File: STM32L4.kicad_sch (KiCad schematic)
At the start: 37 parts, among them J1 Conn_01x04_Pin, U20 TCAN334GDCNT, U21 STM32L496RGTx, U8 TCAN334GDCNT, U9 MR20H40, Y1 8 MHZ Oscillator

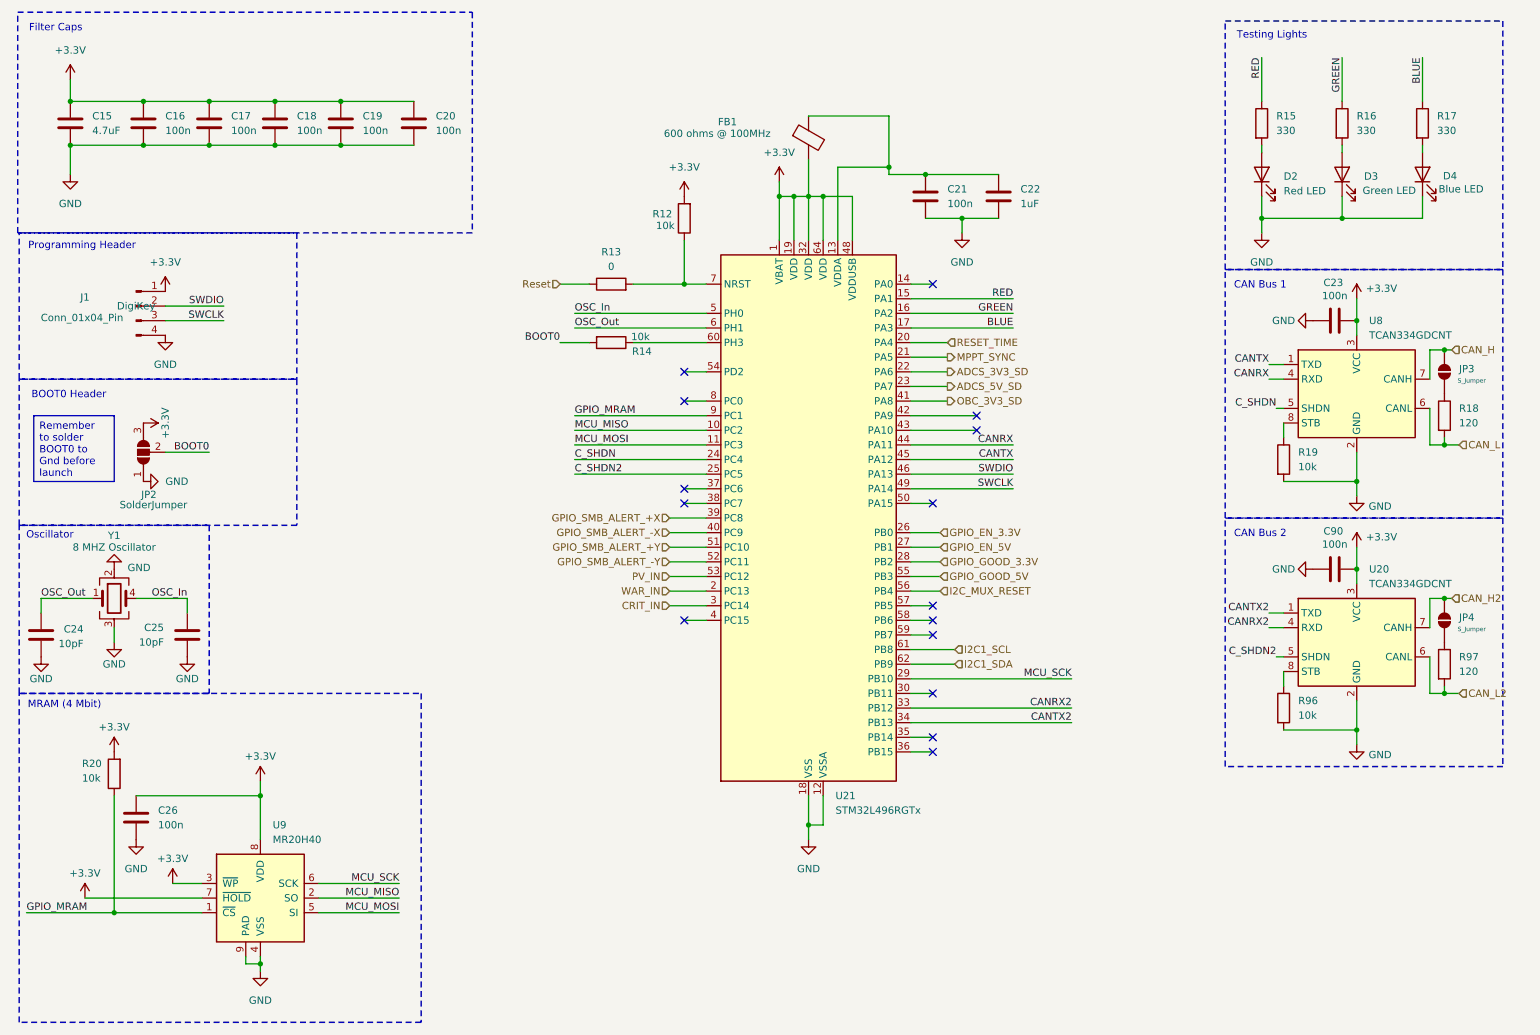
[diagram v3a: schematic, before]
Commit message: Changed LTC 4412 to 4417, still kinks to work out
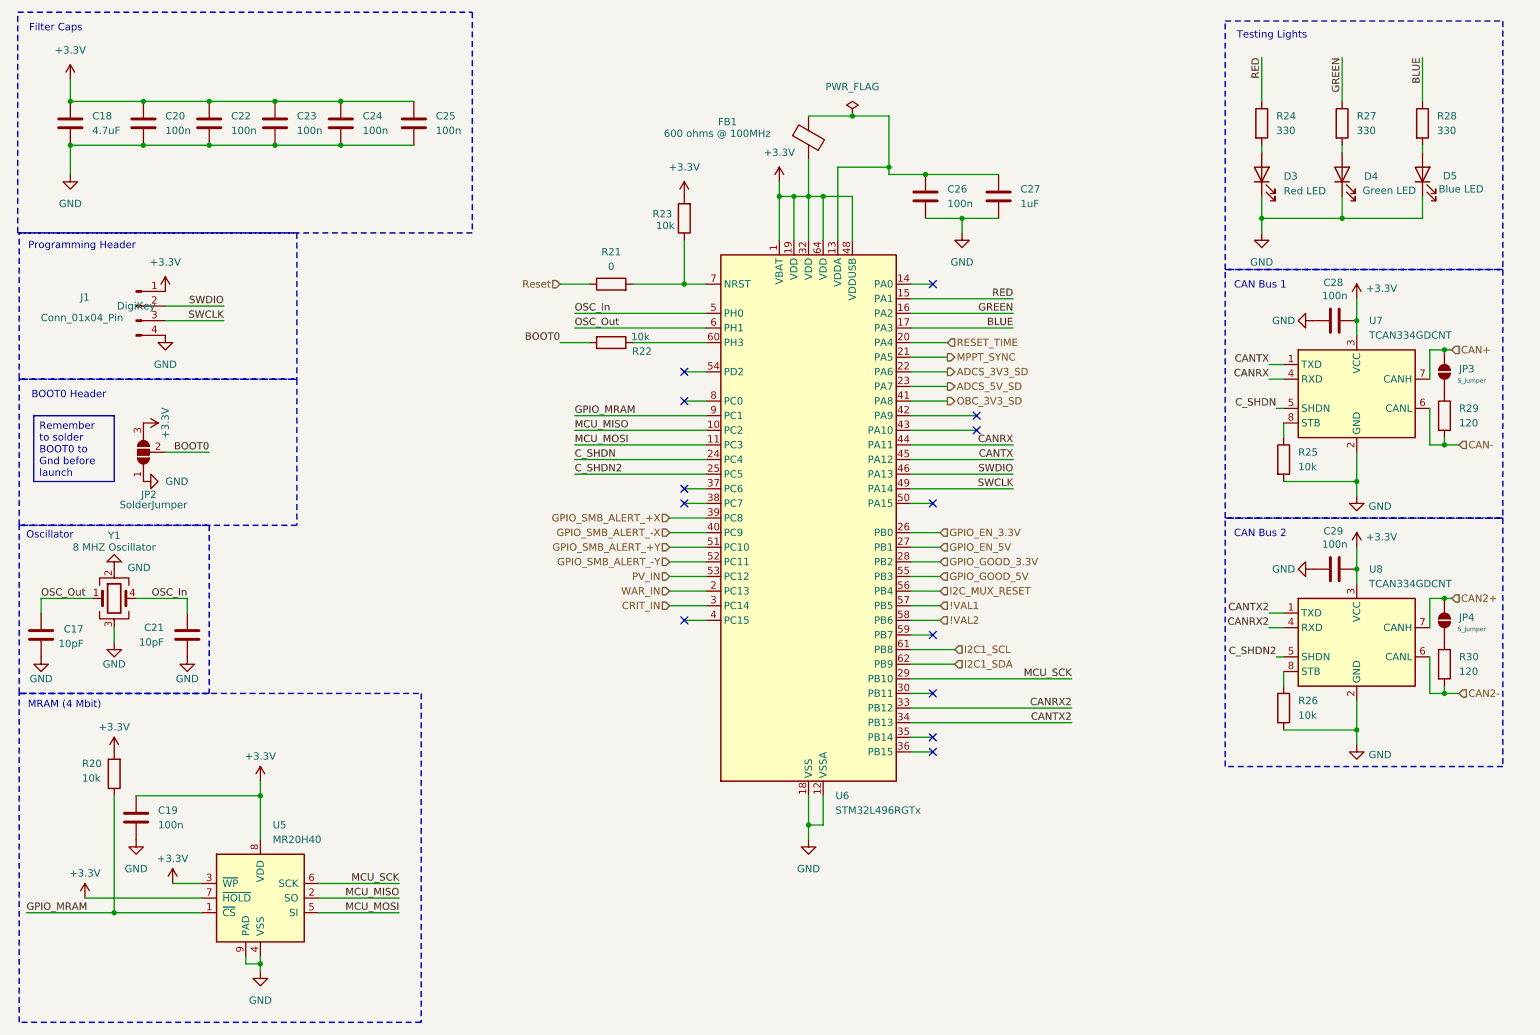
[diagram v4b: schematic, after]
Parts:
- renumbered C24 to C17, C15 to C18, C26 to C19, C16 to C20, C25 to C21, C17 to C22, C18 to C23, C19 to C24, C20 to C25, C21 to C26, C22 to C27, C23 to C28, C90 to C29, D2 to D3, D3 to D4, D4 to D5, R13 to R21, R14 to R22, R12 to R23, R15 to R24, R19 to R25, R96 to R26, R16 to R27, R17 to R28, R18 to R29, R97 to R30, U9 to U5, U21 to U6, U8 to U7, U20 to U8
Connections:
- net !VAL1: now reaches U6.57 (PB5)
- net !VAL2: now reaches U6.58 (PB6)
- net CAN_H renamed CAN+
- net CAN_H2 renamed CAN2+
- net CAN_L renamed CAN-
- net CAN_L2 renamed CAN2-
- no-connect marks 15 -> 13

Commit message: Started PCB layout
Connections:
- net !GPIO_EN_OR_-Y: now reaches U6.30 (PB11)
- net !GPIO_OR_GOOD_+X: now reaches U6.37 (PC6)
- net !GPIO_OR_GOOD_-X: now reaches U6.38 (PC7)
- net !GPIO_OR_GOOD_+Y: now reaches U6.42 (PA9)
- net !GPIO_OR_GOOD_-Y: now reaches U6.43 (PA10)
- net !GPIO_EN_OR_+Y: now reaches U6.59 (PB7)
- net GPIO_EN_3.3V renamed !GPIO_EN_OR_+X
- net GPIO_EN_5V renamed !GPIO_EN_OR_-X
- no-connect marks 13 -> 7
